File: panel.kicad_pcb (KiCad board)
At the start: 2 copper layers, 131.4 x 94 mm, 112 parts, among them J1 Conn_01x05, J2 Conn_01x05, J3 Screw_Terminal

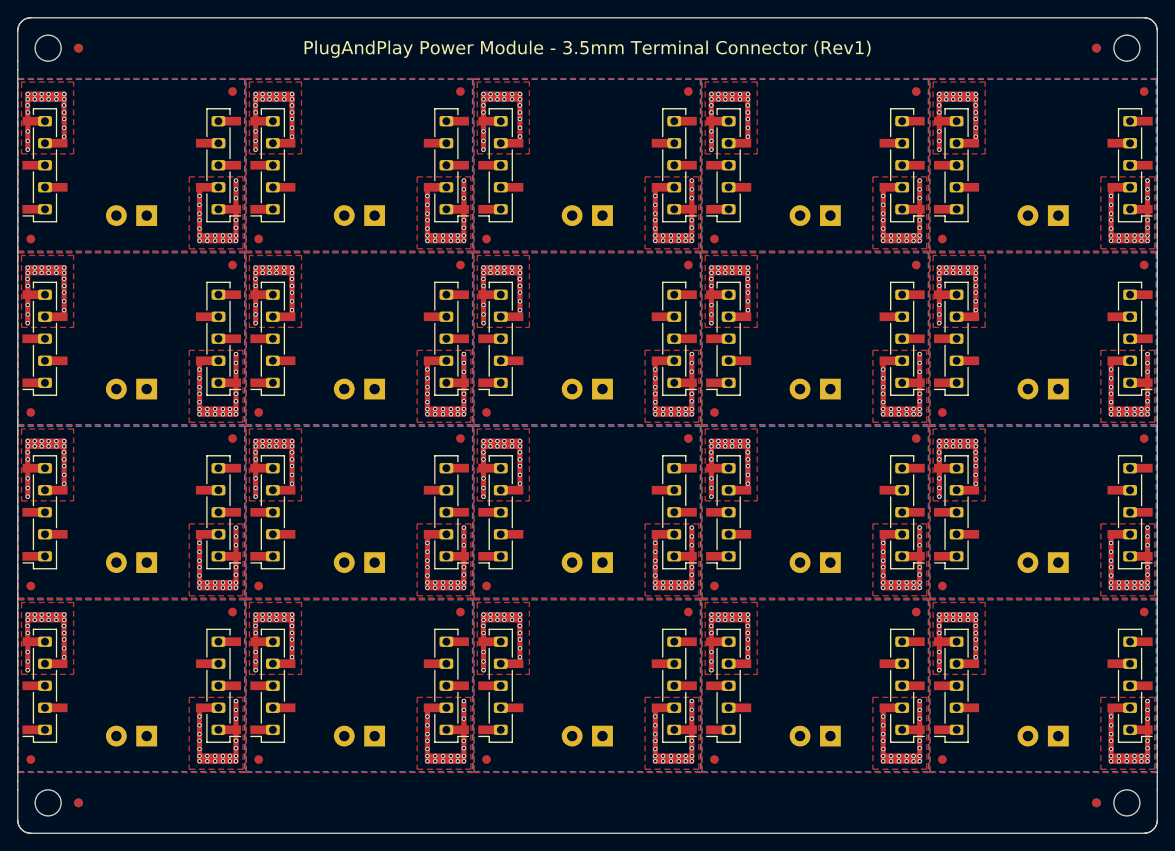
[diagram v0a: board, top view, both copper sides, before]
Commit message: Fix the wrong side connectors
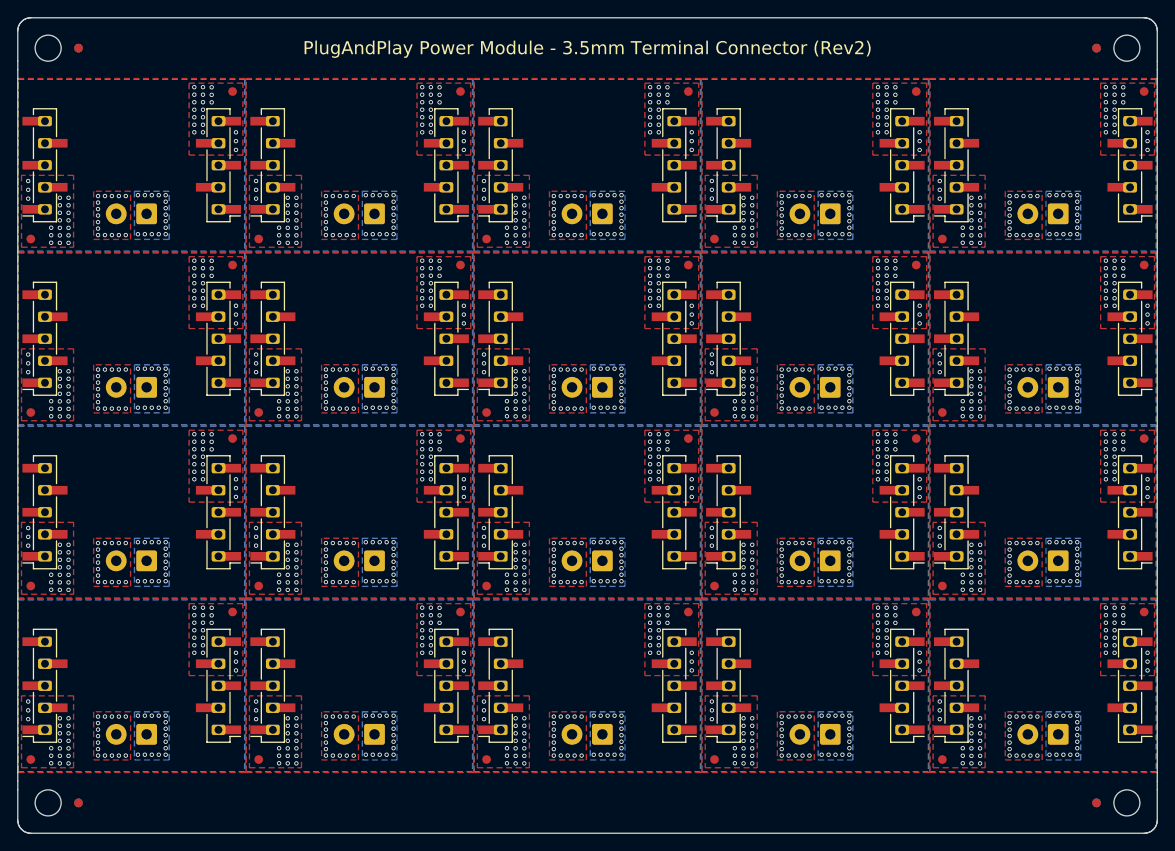
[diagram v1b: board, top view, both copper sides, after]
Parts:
- removed the J3 at (97.7, 102.8)
- removed the J3 at (176.5, 102.8)
- removed the J3 at (150.2, 42.8)
- removed the J3 at (150.2, 102.8)
- removed the J3 at (176.5, 62.8)
- removed the J3 at (202.8, 62.8)
- removed the J3 at (202.8, 82.8)
- removed the J3 at (150.2, 62.8)
- removed the J3 at (97.7, 82.8)
- removed the J3 at (176.5, 82.8)
- removed the J3 at (124.0, 62.8)
- removed the J3 at (202.8, 42.8)
- removed the J3 at (97.7, 42.8)
- removed the J3 at (124.0, 82.8)
- removed the J3 at (150.2, 82.8)
- removed the J3 at (202.8, 102.8)
- removed the J3 at (124.0, 42.8)
- removed the J3 at (97.7, 62.8)
- removed the J3 at (176.5, 42.8)
- removed the J3 at (124.0, 102.8)
- added J3: Screw_Terminal, TerminalBlock_4Ucon:TerminalBlock_4Ucon_1x02_P3.50mm_Horizontal, B.Cu at (202.8, 82.6)
- added J3: Screw_Terminal, TerminalBlock_4Ucon:TerminalBlock_4Ucon_1x02_P3.50mm_Horizontal, B.Cu at (123.9, 42.6)
- added J3: Screw_Terminal, TerminalBlock_4Ucon:TerminalBlock_4Ucon_1x02_P3.50mm_Horizontal, B.Cu at (202.8, 42.6)
- added J3: Screw_Terminal, TerminalBlock_4Ucon:TerminalBlock_4Ucon_1x02_P3.50mm_Horizontal, B.Cu at (202.8, 62.6)
- added J3: Screw_Terminal, TerminalBlock_4Ucon:TerminalBlock_4Ucon_1x02_P3.50mm_Horizontal, B.Cu at (202.8, 102.6)
- added J3: Screw_Terminal, TerminalBlock_4Ucon:TerminalBlock_4Ucon_1x02_P3.50mm_Horizontal, B.Cu at (150.2, 102.6)
- added J3: Screw_Terminal, TerminalBlock_4Ucon:TerminalBlock_4Ucon_1x02_P3.50mm_Horizontal, B.Cu at (176.5, 102.6)
- added J3: Screw_Terminal, TerminalBlock_4Ucon:TerminalBlock_4Ucon_1x02_P3.50mm_Horizontal, B.Cu at (123.9, 102.6)
- added J3: Screw_Terminal, TerminalBlock_4Ucon:TerminalBlock_4Ucon_1x02_P3.50mm_Horizontal, B.Cu at (150.2, 82.6)
- added J3: Screw_Terminal, TerminalBlock_4Ucon:TerminalBlock_4Ucon_1x02_P3.50mm_Horizontal, B.Cu at (123.9, 62.6)
- added J3: Screw_Terminal, TerminalBlock_4Ucon:TerminalBlock_4Ucon_1x02_P3.50mm_Horizontal, B.Cu at (176.5, 42.6)
- added J3: Screw_Terminal, TerminalBlock_4Ucon:TerminalBlock_4Ucon_1x02_P3.50mm_Horizontal, B.Cu at (150.2, 42.6)
- added J3: Screw_Terminal, TerminalBlock_4Ucon:TerminalBlock_4Ucon_1x02_P3.50mm_Horizontal, B.Cu at (97.7, 82.6)
- added J3: Screw_Terminal, TerminalBlock_4Ucon:TerminalBlock_4Ucon_1x02_P3.50mm_Horizontal, B.Cu at (123.9, 82.6)
- added J3: Screw_Terminal, TerminalBlock_4Ucon:TerminalBlock_4Ucon_1x02_P3.50mm_Horizontal, B.Cu at (176.5, 82.6)
- added J3: Screw_Terminal, TerminalBlock_4Ucon:TerminalBlock_4Ucon_1x02_P3.50mm_Horizontal, B.Cu at (176.5, 62.6)
- added J3: Screw_Terminal, TerminalBlock_4Ucon:TerminalBlock_4Ucon_1x02_P3.50mm_Horizontal, B.Cu at (150.2, 62.6)
- added J3: Screw_Terminal, TerminalBlock_4Ucon:TerminalBlock_4Ucon_1x02_P3.50mm_Horizontal, B.Cu at (97.7, 62.6)
- added J3: Screw_Terminal, TerminalBlock_4Ucon:TerminalBlock_4Ucon_1x02_P3.50mm_Horizontal, B.Cu at (97.7, 102.6)
- added J3: Screw_Terminal, TerminalBlock_4Ucon:TerminalBlock_4Ucon_1x02_P3.50mm_Horizontal, B.Cu at (97.7, 42.6)
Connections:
- net Board_0-unconnected-(J1-Pin_3-Pad3) renamed Board_0-unconnected-(J1-Pin_3-Pad3)_1
- net Board_1-unconnected-(J1-Pin_3-Pad3) renamed Board_1-unconnected-(J1-Pin_3-Pad3)_1
- net Board_10-unconnected-(J1-Pin_3-Pad3) renamed Board_10-unconnected-(J1-Pin_3-Pad3)_1
- net Board_11-unconnected-(J1-Pin_3-Pad3) renamed Board_11-unconnected-(J1-Pin_3-Pad3)_1
- net Board_12-unconnected-(J1-Pin_3-Pad3) renamed Board_12-unconnected-(J1-Pin_3-Pad3)_1
- net Board_13-unconnected-(J1-Pin_3-Pad3) renamed Board_13-unconnected-(J1-Pin_3-Pad3)_1
- net Board_14-unconnected-(J1-Pin_3-Pad3) renamed Board_14-unconnected-(J1-Pin_3-Pad3)_1
- net Board_15-unconnected-(J1-Pin_3-Pad3) renamed Board_15-unconnected-(J1-Pin_3-Pad3)_1
- net Board_16-unconnected-(J1-Pin_3-Pad3) renamed Board_16-unconnected-(J1-Pin_3-Pad3)_1
- net Board_17-unconnected-(J1-Pin_3-Pad3) renamed Board_17-unconnected-(J1-Pin_3-Pad3)_1
- net Board_18-unconnected-(J1-Pin_3-Pad3) renamed Board_18-unconnected-(J1-Pin_3-Pad3)_1
- net Board_19-unconnected-(J1-Pin_3-Pad3) renamed Board_19-unconnected-(J1-Pin_3-Pad3)_1
- net Board_2-unconnected-(J1-Pin_3-Pad3) renamed Board_2-unconnected-(J1-Pin_3-Pad3)_1
- net Board_3-unconnected-(J1-Pin_3-Pad3) renamed Board_3-unconnected-(J1-Pin_3-Pad3)_1
- net Board_4-unconnected-(J1-Pin_3-Pad3) renamed Board_4-unconnected-(J1-Pin_3-Pad3)_1
- net Board_5-unconnected-(J1-Pin_3-Pad3) renamed Board_5-unconnected-(J1-Pin_3-Pad3)_1
- net Board_6-unconnected-(J1-Pin_3-Pad3) renamed Board_6-unconnected-(J1-Pin_3-Pad3)_1
- net Board_7-unconnected-(J1-Pin_3-Pad3) renamed Board_7-unconnected-(J1-Pin_3-Pad3)_1
- net Board_8-unconnected-(J1-Pin_3-Pad3) renamed Board_8-unconnected-(J1-Pin_3-Pad3)_1
- net Board_9-unconnected-(J1-Pin_3-Pad3) renamed Board_9-unconnected-(J1-Pin_3-Pad3)_1
- J1 pad 1: Board_17-VDC -> Board_17-GND
- J1 pad 2: Board_17-VDC -> Board_17-GND
- J1 pad 4: Board_17-GND -> Board_17-VDC
- J1 pad 5: Board_17-GND -> Board_17-VDC
- J1 pad 1: Board_1-VDC -> Board_1-GND
- J1 pad 2: Board_1-VDC -> Board_1-GND
- J1 pad 4: Board_1-GND -> Board_1-VDC
- J1 pad 5: Board_1-GND -> Board_1-VDC
- J1 pad 1: Board_11-VDC -> Board_11-GND
- J1 pad 2: Board_11-VDC -> Board_11-GND
- J1 pad 4: Board_11-GND -> Board_11-VDC
- J1 pad 5: Board_11-GND -> Board_11-VDC
- J1 pad 1: Board_19-VDC -> Board_19-GND
- J1 pad 2: Board_19-VDC -> Board_19-GND
- J1 pad 4: Board_19-GND -> Board_19-VDC
- J1 pad 5: Board_19-GND -> Board_19-VDC
- J1 pad 1: Board_4-VDC -> Board_4-GND
- J1 pad 2: Board_4-VDC -> Board_4-GND
- J1 pad 4: Board_4-GND -> Board_4-VDC
- J1 pad 5: Board_4-GND -> Board_4-VDC
- J1 pad 1: Board_16-VDC -> Board_16-GND
- J1 pad 2: Board_16-VDC -> Board_16-GND
- J1 pad 4: Board_16-GND -> Board_16-VDC
- J1 pad 5: Board_16-GND -> Board_16-VDC
- J1 pad 1: Board_12-VDC -> Board_12-GND
- J1 pad 2: Board_12-VDC -> Board_12-GND
- J1 pad 4: Board_12-GND -> Board_12-VDC
- J1 pad 5: Board_12-GND -> Board_12-VDC
- J1 pad 1: Board_14-VDC -> Board_14-GND
- J1 pad 2: Board_14-VDC -> Board_14-GND
- J1 pad 4: Board_14-GND -> Board_14-VDC
- J1 pad 5: Board_14-GND -> Board_14-VDC
- J1 pad 1: Board_18-VDC -> Board_18-GND
- J1 pad 2: Board_18-VDC -> Board_18-GND
- J1 pad 4: Board_18-GND -> Board_18-VDC
- J1 pad 5: Board_18-GND -> Board_18-VDC
- J1 pad 1: Board_5-VDC -> Board_5-GND
- J1 pad 2: Board_5-VDC -> Board_5-GND
- J1 pad 4: Board_5-GND -> Board_5-VDC
- J1 pad 5: Board_5-GND -> Board_5-VDC
- J1 pad 1: Board_13-VDC -> Board_13-GND
- J1 pad 2: Board_13-VDC -> Board_13-GND
- J1 pad 4: Board_13-GND -> Board_13-VDC
- J1 pad 5: Board_13-GND -> Board_13-VDC
- J1 pad 1: Board_15-VDC -> Board_15-GND
- J1 pad 2: Board_15-VDC -> Board_15-GND
- J1 pad 4: Board_15-GND -> Board_15-VDC
- J1 pad 5: Board_15-GND -> Board_15-VDC
- J1 pad 1: Board_3-VDC -> Board_3-GND
- J1 pad 2: Board_3-VDC -> Board_3-GND
- J1 pad 4: Board_3-GND -> Board_3-VDC
- J1 pad 5: Board_3-GND -> Board_3-VDC
- J1 pad 1: Board_2-VDC -> Board_2-GND
- J1 pad 2: Board_2-VDC -> Board_2-GND
- J1 pad 4: Board_2-GND -> Board_2-VDC
- J1 pad 5: Board_2-GND -> Board_2-VDC
- J1 pad 1: Board_8-VDC -> Board_8-GND
- J1 pad 2: Board_8-VDC -> Board_8-GND
- J1 pad 4: Board_8-GND -> Board_8-VDC
- J1 pad 5: Board_8-GND -> Board_8-VDC
- J1 pad 1: Board_9-VDC -> Board_9-GND
- J1 pad 2: Board_9-VDC -> Board_9-GND
- J1 pad 4: Board_9-GND -> Board_9-VDC
- J1 pad 5: Board_9-GND -> Board_9-VDC
- J1 pad 1: Board_10-VDC -> Board_10-GND
- J1 pad 2: Board_10-VDC -> Board_10-GND
- J1 pad 4: Board_10-GND -> Board_10-VDC
- J1 pad 5: Board_10-GND -> Board_10-VDC
- J1 pad 1: Board_0-VDC -> Board_0-GND
- J1 pad 2: Board_0-VDC -> Board_0-GND
- J1 pad 4: Board_0-GND -> Board_0-VDC
- J1 pad 5: Board_0-GND -> Board_0-VDC
- J1 pad 1: Board_6-VDC -> Board_6-GND
- J1 pad 2: Board_6-VDC -> Board_6-GND
- J1 pad 4: Board_6-GND -> Board_6-VDC
- J1 pad 5: Board_6-GND -> Board_6-VDC
- J1 pad 1: Board_7-VDC -> Board_7-GND
- J1 pad 2: Board_7-VDC -> Board_7-GND
- J1 pad 4: Board_7-GND -> Board_7-VDC
- J1 pad 5: Board_7-GND -> Board_7-VDC
- J2 pad 1: Board_19-GND -> Board_19-VDC
- J2 pad 2: Board_19-GND -> Board_19-VDC
- J2 pad 4: Board_19-VDC -> Board_19-GND
- J2 pad 5: Board_19-VDC -> Board_19-GND
- J2 pad 1: Board_5-GND -> Board_5-VDC
- J2 pad 2: Board_5-GND -> Board_5-VDC
- J2 pad 4: Board_5-VDC -> Board_5-GND
- J2 pad 5: Board_5-VDC -> Board_5-GND
- J2 pad 1: Board_8-GND -> Board_8-VDC
- J2 pad 2: Board_8-GND -> Board_8-VDC
- J2 pad 4: Board_8-VDC -> Board_8-GND
- J2 pad 5: Board_8-VDC -> Board_8-GND
- J2 pad 1: Board_18-GND -> Board_18-VDC
- J2 pad 2: Board_18-GND -> Board_18-VDC
- J2 pad 4: Board_18-VDC -> Board_18-GND
- J2 pad 5: Board_18-VDC -> Board_18-GND
- J2 pad 1: Board_17-GND -> Board_17-VDC
- J2 pad 2: Board_17-GND -> Board_17-VDC
- J2 pad 4: Board_17-VDC -> Board_17-GND
- J2 pad 5: Board_17-VDC -> Board_17-GND
- J2 pad 1: Board_9-GND -> Board_9-VDC
- J2 pad 2: Board_9-GND -> Board_9-VDC
- J2 pad 4: Board_9-VDC -> Board_9-GND
- J2 pad 5: Board_9-VDC -> Board_9-GND
- J2 pad 1: Board_6-GND -> Board_6-VDC
- J2 pad 2: Board_6-GND -> Board_6-VDC
- J2 pad 4: Board_6-VDC -> Board_6-GND
- J2 pad 5: Board_6-VDC -> Board_6-GND
- J2 pad 1: Board_2-GND -> Board_2-VDC
- J2 pad 2: Board_2-GND -> Board_2-VDC
- J2 pad 4: Board_2-VDC -> Board_2-GND
- J2 pad 5: Board_2-VDC -> Board_2-GND
- J2 pad 1: Board_13-GND -> Board_13-VDC
- J2 pad 2: Board_13-GND -> Board_13-VDC
- J2 pad 4: Board_13-VDC -> Board_13-GND
- J2 pad 5: Board_13-VDC -> Board_13-GND
- J2 pad 1: Board_14-GND -> Board_14-VDC
- J2 pad 2: Board_14-GND -> Board_14-VDC
- J2 pad 4: Board_14-VDC -> Board_14-GND
- J2 pad 5: Board_14-VDC -> Board_14-GND
- J2 pad 1: Board_1-GND -> Board_1-VDC
- J2 pad 2: Board_1-GND -> Board_1-VDC
- J2 pad 4: Board_1-VDC -> Board_1-GND
- J2 pad 5: Board_1-VDC -> Board_1-GND
- J2 pad 1: Board_10-GND -> Board_10-VDC
- J2 pad 2: Board_10-GND -> Board_10-VDC
- J2 pad 4: Board_10-VDC -> Board_10-GND
- J2 pad 5: Board_10-VDC -> Board_10-GND
- J2 pad 1: Board_11-GND -> Board_11-VDC
- J2 pad 2: Board_11-GND -> Board_11-VDC
- J2 pad 4: Board_11-VDC -> Board_11-GND
- J2 pad 5: Board_11-VDC -> Board_11-GND
- J2 pad 1: Board_3-GND -> Board_3-VDC
- J2 pad 2: Board_3-GND -> Board_3-VDC
- J2 pad 4: Board_3-VDC -> Board_3-GND
- J2 pad 5: Board_3-VDC -> Board_3-GND
- J2 pad 1: Board_4-GND -> Board_4-VDC
- J2 pad 2: Board_4-GND -> Board_4-VDC
- J2 pad 4: Board_4-VDC -> Board_4-GND
- J2 pad 5: Board_4-VDC -> Board_4-GND
- J2 pad 1: Board_15-GND -> Board_15-VDC
- J2 pad 2: Board_15-GND -> Board_15-VDC
- J2 pad 4: Board_15-VDC -> Board_15-GND
- J2 pad 5: Board_15-VDC -> Board_15-GND
- J2 pad 1: Board_16-GND -> Board_16-VDC
- J2 pad 2: Board_16-GND -> Board_16-VDC
- J2 pad 4: Board_16-VDC -> Board_16-GND
- J2 pad 5: Board_16-VDC -> Board_16-GND
- J2 pad 1: Board_7-GND -> Board_7-VDC
- J2 pad 2: Board_7-GND -> Board_7-VDC
- J2 pad 4: Board_7-VDC -> Board_7-GND
- J2 pad 5: Board_7-VDC -> Board_7-GND
- J2 pad 1: Board_12-GND -> Board_12-VDC
- J2 pad 2: Board_12-GND -> Board_12-VDC
- J2 pad 4: Board_12-VDC -> Board_12-GND
- J2 pad 5: Board_12-VDC -> Board_12-GND
- J2 pad 1: Board_0-GND -> Board_0-VDC
- J2 pad 2: Board_0-GND -> Board_0-VDC
- J2 pad 4: Board_0-VDC -> Board_0-GND
- J2 pad 5: Board_0-VDC -> Board_0-GND
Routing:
- net Board_19-GND: track 41.8 -> 0.00 mm, vias 44 -> 55
- net Board_18-GND: track 41.8 -> 0.00 mm, vias 44 -> 55
- net Board_14-GND: track 41.8 -> 0.00 mm, vias 44 -> 55
- net Board_13-GND: track 41.8 -> 0.00 mm, vias 44 -> 55
- net Board_16-GND: track 41.8 -> 0.00 mm, vias 44 -> 55
- net Board_11-GND: track 41.8 -> 0.00 mm, vias 44 -> 55
- net Board_12-GND: track 41.8 -> 0.00 mm, vias 44 -> 55
- net Board_17-GND: track 41.8 -> 0.00 mm, vias 44 -> 55
- net Board_4-GND: track 41.8 -> 0.00 mm, vias 44 -> 55
- net Board_3-GND: track 41.8 -> 0.00 mm, vias 44 -> 55
- net Board_9-GND: track 41.8 -> 0.00 mm, vias 44 -> 55
- net Board_8-GND: track 41.8 -> 0.00 mm, vias 44 -> 55
- net Board_6-GND: track 41.8 -> 0.00 mm, vias 44 -> 55
- net Board_15-GND: track 41.8 -> 0.00 mm, vias 44 -> 55
- net Board_10-GND: track 41.8 -> 0.00 mm, vias 44 -> 55
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- added copper zone on B.Cu, net Board_0-VDC
- added copper zone on B.Cu, net Board_1-VDC
- added copper zone on B.Cu, net Board_10-VDC
- added copper zone on B.Cu, net Board_11-VDC
- added copper zone on B.Cu, net Board_12-VDC
- added copper zone on B.Cu, net Board_13-VDC
- added copper zone on B.Cu, net Board_14-VDC
- added copper zone on B.Cu, net Board_15-VDC
- added copper zone on B.Cu, net Board_16-VDC
- added copper zone on B.Cu, net Board_17-VDC
- added copper zone on B.Cu, net Board_18-VDC
- added copper zone on B.Cu, net Board_19-VDC
- added copper zone on B.Cu, net Board_2-VDC
- added copper zone on B.Cu, net Board_3-VDC
- added copper zone on B.Cu, net Board_4-VDC
- added copper zone on B.Cu, net Board_5-VDC
- added copper zone on B.Cu, net Board_6-VDC
- added copper zone on B.Cu, net Board_7-VDC
- added copper zone on B.Cu, net Board_8-VDC
- added copper zone on B.Cu, net Board_9-VDC
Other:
- board text added: "PlugAndPlay Power Module - 3.5mm Terminal Connector (Rev2)"
- board text added: "PnP Power Module 3.5mm Screw Terminal"
- board text removed: "PlugAndPlay Power Module - 3.5mm Terminal Connector (Rev1)"
- board text removed: "PnP Power Module Screw Terminal"
